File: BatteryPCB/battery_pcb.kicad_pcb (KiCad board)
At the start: 2 copper layers, 145.3 x 142.5 mm, 46 parts, among them J1 ESP32 left, J2 ESP32 right, J3 RunCam Split 4, J5 to COTS altimeter, J6 to SRAD flight computer, SW1 CAM POWER, SW2 COTS ARM, SW3 SRAD ARM, U1 LMR51430XFDDCR

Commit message: Battery PCB v17: test points, strict design rules, review fixes
- Test points: TP1 +5V (buck output), TP2 VBAT+ (2S pack), TP3/TP4 GND;
  2 mm through-hole pads placed where both sides are open
- Strict rules in the project: 0.25/0.3/0.4 mm clearance (signal/power/pyro),
  0.3 mm hole clearance, 0.5 mm hole-to-hole, 0.15 mm via ring, silk spacing;
  every DRC check is an error. Fixed the spots they flagged around U1, R4, C8,
  D1/D3 silk and the TP4 label
- R5 47k -> 39k so VBAT_SENSE stays inside the ESP32 ADC range at a full pack
- BOM note: the RunCam needs a built harness (3-pin power/video + RX/TX pads)
- README: exact ESP32 to buy (ESP32-DevKitC-32E, not WROVER or 30-pin clones),
  design rules, sense scaling; layout notes for v17
- Checks: ERC 0 errors; DRC 0 violations incl. warnings with schematic parity;
  all 115 schematic pins match board pad nets; verify_A ALL PASS

Co-Authored-By: Claude Opus 5.5 <noreply@anthropic.com>
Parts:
- added TP1: TP_5V, TestPoint:TestPoint_THTPad_D2.0mm_Drill1.0mm, F.Cu at (173.8, 166.0)
- added TP2: TP_VBAT, TestPoint:TestPoint_THTPad_D2.0mm_Drill1.0mm, F.Cu at (113.5, 199.5)
- added TP3: TP_GND, TestPoint:TestPoint_THTPad_D2.0mm_Drill1.0mm, F.Cu at (173.8, 170.5)
- added TP4: TP_GND, TestPoint:TestPoint_THTPad_D2.0mm_Drill1.0mm, F.Cu at (109.5, 199.5)
- R5: value 47k -> 39k
- moved D3 0.20 mm to (154.7, 154.3)
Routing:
- net /2. Buck to 5 V/+5V: track 88.7 -> 94.1 mm
- net /1. Battery 2S + protection/VBAT+: track 0.00 -> 5.06 mm
- net /3. Pack voltage sense/VBAT_SENSE: track 31.0 -> 33.3 mm
- net GND: vias 109 -> 107
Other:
- board text added: "VBAT"

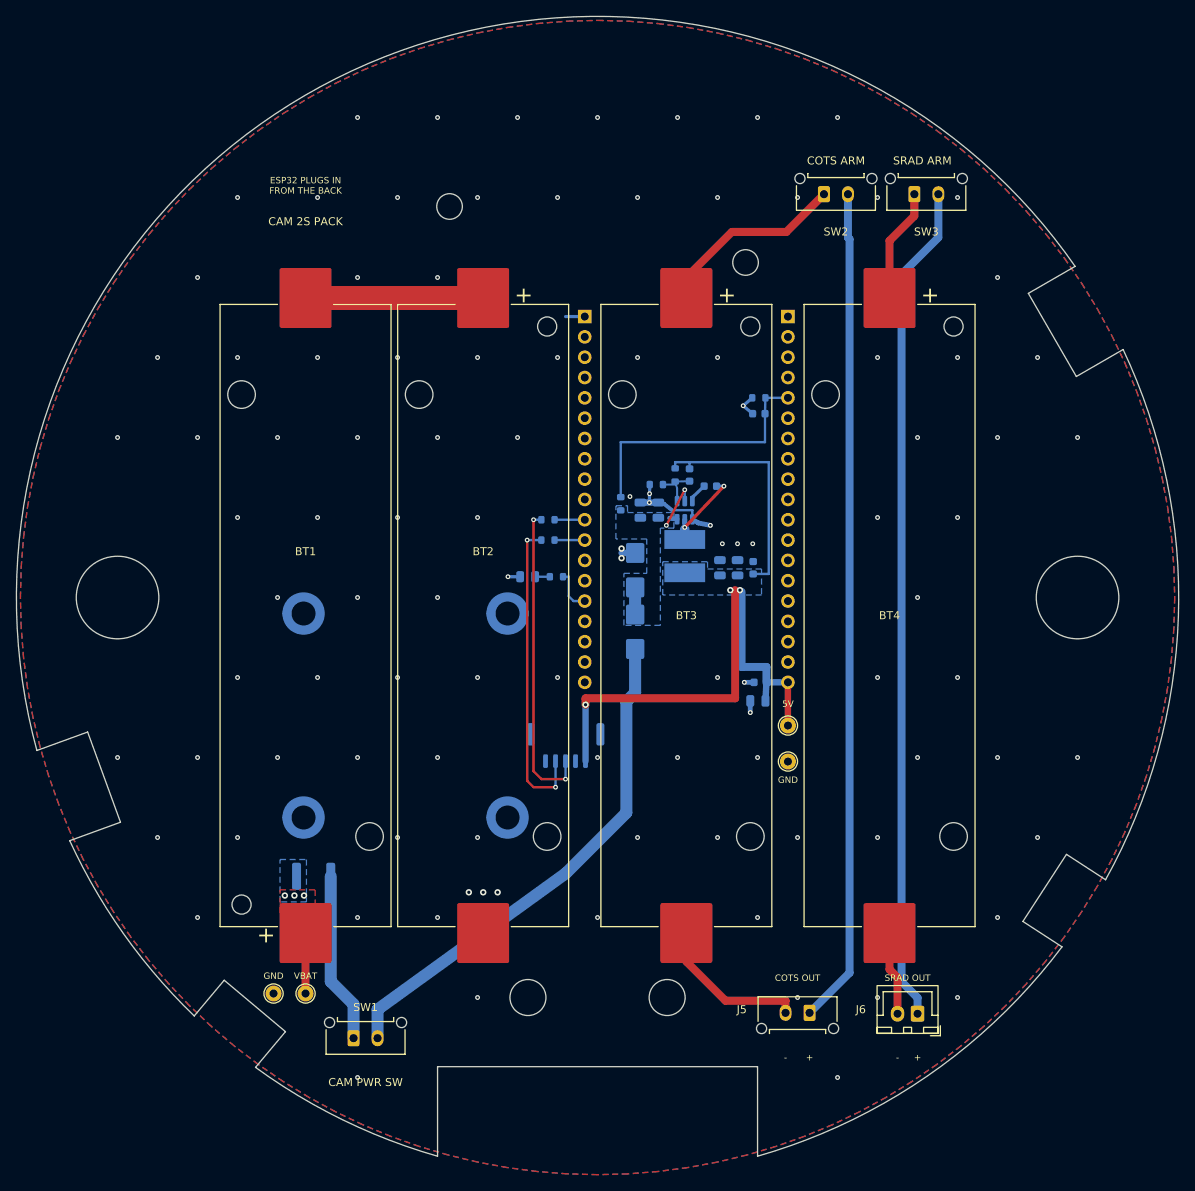
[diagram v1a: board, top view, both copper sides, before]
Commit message: Battery PCB v18: antenna clearance, stack outline, cut-outs, XT30 outputs
Second design review:
- ESP32 antenna: back-copper keep-out (no pour, tracks or vias) 15 mm to
  each side of and past the DevKitC antenna, outlined on the back silk;
  COTS_SW rerouted around it; nylon M3 note for H5, the stack bolt over it.
- Pin-switch stack outlined on the front silk.
- Two spare 12 x 7 mm wire pass-throughs at the upper left.
- J5/J6 battery outputs are AMASS XT30UPB-F (pin 1 minus, pin 2 plus);
  schematic labels swapped to match, BOM and cable-side parts updated.
ERC 0 errors, DRC 0 (strict, schematic parity), verify_A all pass.

Co-Authored-By: Claude Opus 5.5 <noreply@anthropic.com>
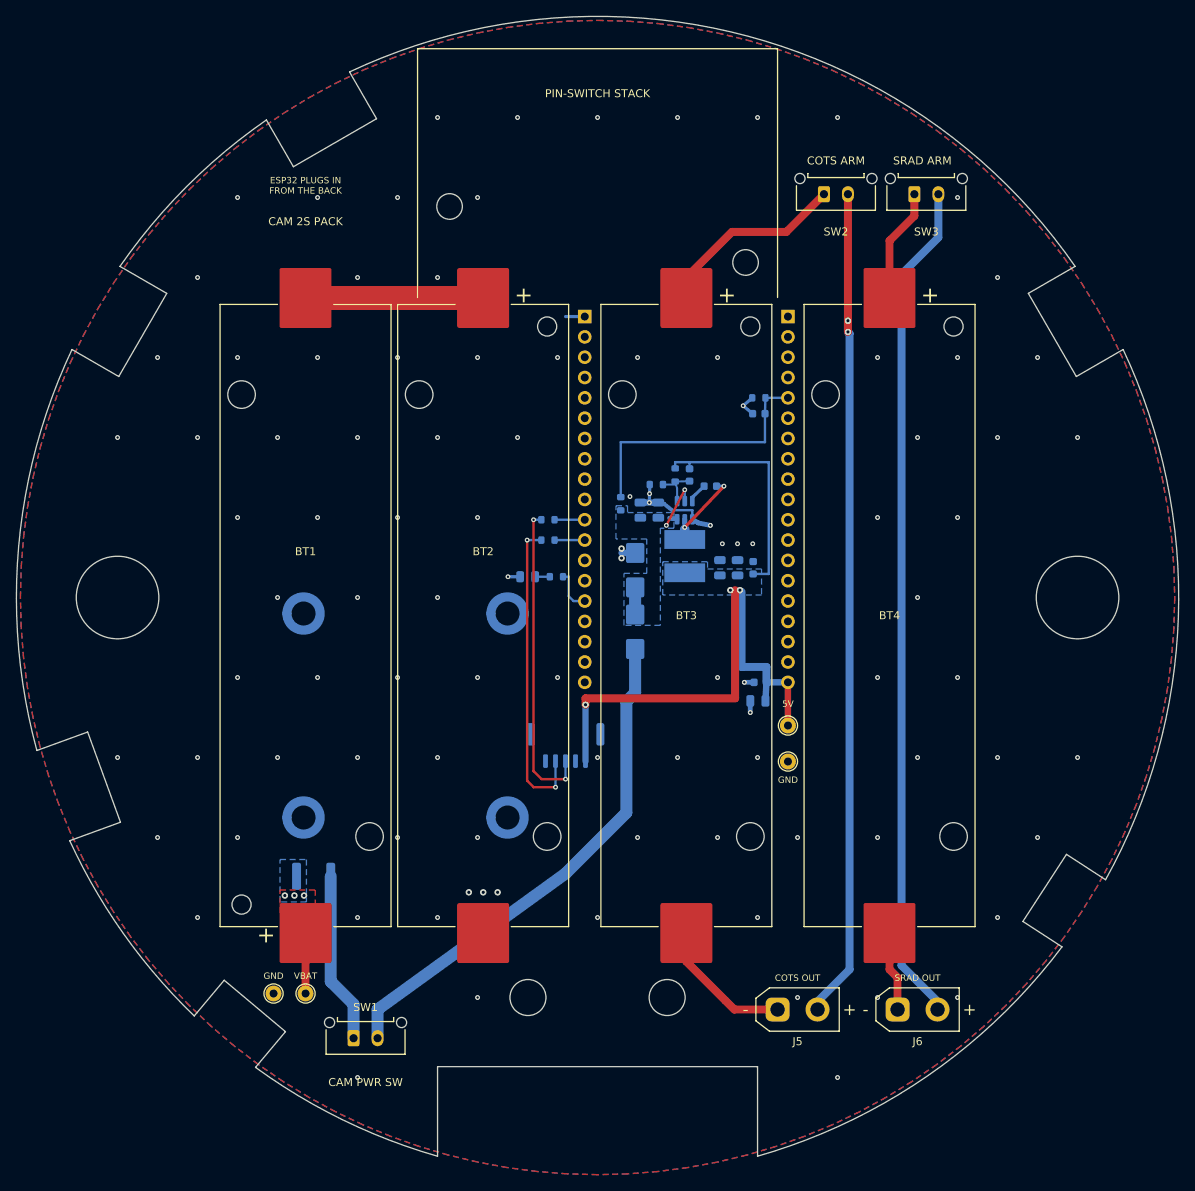
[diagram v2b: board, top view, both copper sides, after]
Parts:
- J5: footprint battery_pcb:Molex_Micro-Fit_3.0_43650-0215_1x02_P3.00mm_Vertical -> battery_pcb:AMASS_XT30UPB-F_1x02_P5.0mm_Vertical
- J6: footprint Connector_JST:JST_XH_B2B-XH-A_1x02_P2.50mm_Vertical -> battery_pcb:AMASS_XT30UPB-F_1x02_P5.0mm_Vertical
- moved J5 4.02 mm to (172.5, 201.5), turned to 0 degrees
- moved J6 2.55 mm to (187.5, 201.5), turned to 0 degrees
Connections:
- J5 pad 1: /6. COTS / SRAD supplies/COTS_SW -> /6. COTS / SRAD supplies/COTS_BAT-
- J5 pad 2: /6. COTS / SRAD supplies/COTS_BAT- -> /6. COTS / SRAD supplies/COTS_SW
- J6 pad 1: /6. COTS / SRAD supplies/SRAD_SW -> /6. COTS / SRAD supplies/SRAD_BAT-
- J6 pad 2: /6. COTS / SRAD supplies/SRAD_BAT- -> /6. COTS / SRAD supplies/SRAD_SW
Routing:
- net /6. COTS / SRAD supplies/COTS_BAT-: track 19.5 -> 17.4 mm
- net /6. COTS / SRAD supplies/COTS_SW: track 104.5 -> 105.1 mm, vias 0 -> 2
- net /6. COTS / SRAD supplies/SRAD_BAT-: track 10.5 -> 9.97 mm
- net /6. COTS / SRAD supplies/SRAD_SW: track 105.2 -> 105.7 mm
- net GND: vias 107 -> 101
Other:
- outline, holes or cut-outs redrawn
- board text added: "ANTENNA KEEP-OUT 15 mm NO COPPER THIS SIDE"
- board text added: "H5: NYLON M3 BOLT AND NUT"
- board text added: "PIN-SWITCH STACK"
- board text removed: "+"
- board text removed: "-"

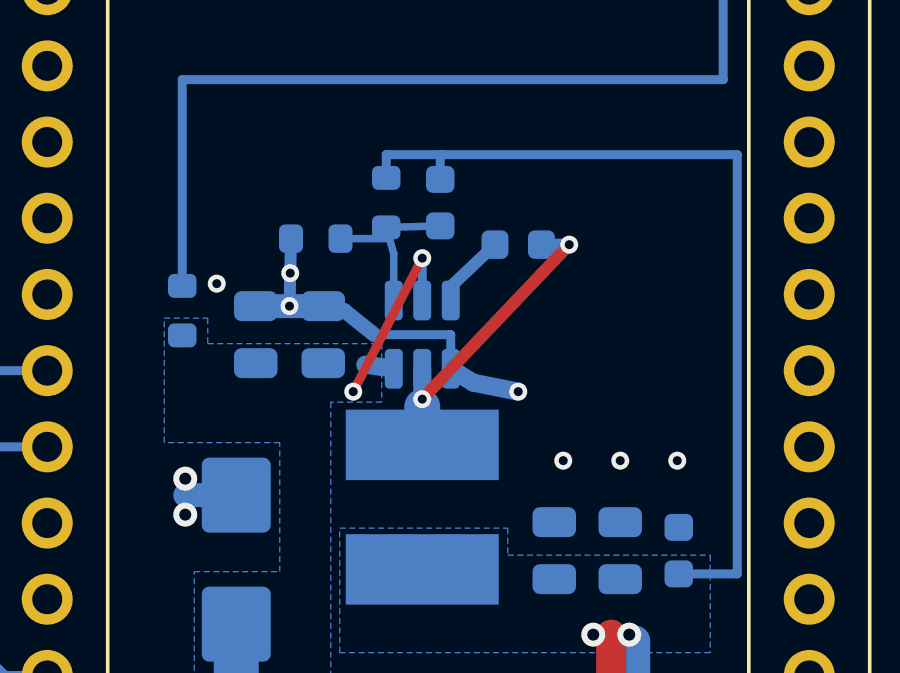
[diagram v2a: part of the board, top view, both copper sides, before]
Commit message: Battery PCB v19: UVLO on the buck, input caps, 6.8 uH, wired schematic
Third review (design check of the power path):
- U1 EN gets an R9/R10 divider (UVLO: on 6.3 V, off 5.5 V at VIN) so
  the 2S pack is no longer run down to 1.8 V per cell.
- Input caps per the LMR51430 datasheet: C1 is the 100 nF at U1's pins,
  C2 + new C11 (10 uF) are the bulk.
- L1 6.8 uH (TI's value for 500 kHz / 5 V out), same footprint.
- Sheets 1-3 redrawn with wires; C1/C2 moved next to U1; stale 47k
  divider note and the SS34 value on D3 corrected.
ERC 0 errors, DRC 0 (strict, schematic parity), verify_A all pass.

Co-Authored-By: Claude Opus 5.5 <noreply@anthropic.com>
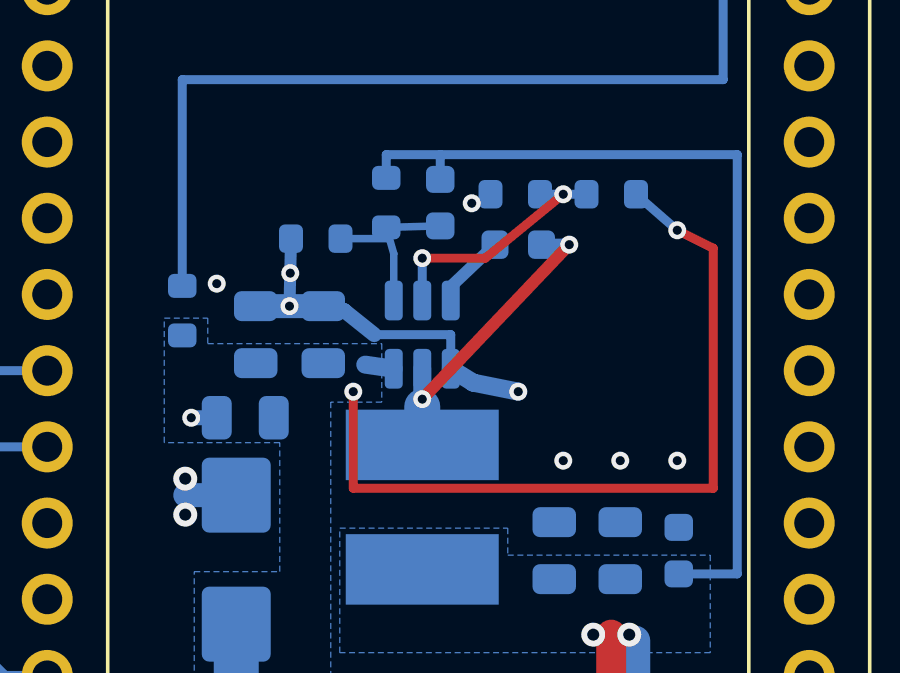
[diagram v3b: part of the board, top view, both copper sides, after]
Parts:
- added C11: 10u / 25V, Capacitor_SMD:C_0805_2012Metric, B.Cu at (155.0, 141.8)
- added R10: 100k 1%, Resistor_SMD:R_0603_1608Metric, B.Cu at (164.0, 134.4)
- added R9: 412k 1%, Resistor_SMD:R_0603_1608Metric, B.Cu at (167.2, 134.4)
- C1: value 10u / 25V -> 100n / 50V
- D3: value SS34 reverse prot -> B340B
- L1: value 4u7 / 3A -> 6u8 / 3.6A
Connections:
- U1 pad 5: /1. Battery 2S + protection/VIN -> /2. Buck to 5 V/EN
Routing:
- net /1. Battery 2S + protection/VIN: track 10.8 -> 30.7 mm
- net /2. Buck to 5 V/EN: track 0.00 -> 8.42 mm, vias 0 -> 2
- net GND: track 24.0 -> 24.8 mm, vias 101 -> 103

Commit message: Battery PCB v19.1: LCSC part numbers, R9 402k (412k out of stock)
- BOM: checked LCSC numbers for every soldered part LCSC sells, DigiKey/
  Mouser numbers for the rest (Keystone 1042, Wurth 9774050243R, ESP32).
  J1/J2 LCSC alternative HCTL PM254-1-19-Z-8.5 (Sullins out of stock).
- JLCPCB assembly BOM + CPL (optional).
- R9 412k -> 402k (412k has no LCSC stock): UVLO on 6.2 V, off 5.4 V.
ERC 0 errors, DRC 0 (strict, schematic parity), verify_A all pass.

Co-Authored-By: Claude Opus 5.5 <noreply@anthropic.com>
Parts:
- R9: value 412k 1% -> 402k 1%
